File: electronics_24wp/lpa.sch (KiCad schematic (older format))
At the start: 26 parts, among them IC1 ATMEGA328-A, P1 CONN_2, P2 CONN_3X2, U1 SD_CARD, U2 LD1117S33, Y1 RESONATEUR

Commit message: Changed names of kicad files.
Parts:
- C1, C2, C3, C4, C5: symbol C-RESCUE-tca -> C-RESCUE-lpa
- ERR1, FIN1, ON1: symbol LED-RESCUE-tca -> LED-RESCUE-lpa
- IC1: symbol ATMEGA328-A-RESCUE-tca -> ATMEGA328-A-RESCUE-lpa
- R1, R15, R16, R17, R18, R19, R2, R_ERR1, R_FIN1, R_ON1: symbol R-RESCUE-tca -> R-RESCUE-lpa
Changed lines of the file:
@@
 EESchema Schematic File Version 2
-LIBS:tca-rescue
+LIBS:lpa-rescue
 LIBS:power
 LIBS:device
@@
 LIBS:valves
 LIBS:myParts
-LIBS:tca-cache
+LIBS:lpa-cache
 EELAYER 25 0
 EELAYER END
@@
 SS
 $Comp
-L GND-RESCUE-tca #PWR01
+L GND-RESCUE-lpa #PWR01
 U 1 1 5358B074
 P 2450 2800
@@
 $EndComp
 $Comp
-L C-RESCUE-tca C5
+L C-RESCUE-lpa C5
 U 1 1 535704C8
 P 3300 6600
@@
 $EndComp
 $Comp
-L C-RESCUE-tca C3
+L C-RESCUE-lpa C3
 U 1 1 535704B9
 P 1550 6600
@@
 ERR
 $Comp
-L R-RESCUE-tca R_FIN1
+L R-RESCUE-lpa R_FIN1
 U 1 1 5356ED9C
 P 4150 6850
@@
 $EndComp
 $Comp
-L R-RESCUE-tca R_ERR1
+L R-RESCUE-lpa R_ERR1
 U 1 1 5356ED8D
 P 4150 6550
@@
 $EndComp
 $Comp
-L R-RESCUE-tca R_ON1
+L R-RESCUE-lpa R_ON1
 U 1 1 5356ED7E
 P 4150 6250
@@
 ERR
 $Comp
-L LED-RESCUE-tca FIN1
+L LED-RESCUE-lpa FIN1
 U 1 1 5356E78D
 P 4750 6850
@@
 $EndComp
 $Comp
-L LED-RESCUE-tca ERR1
+L LED-RESCUE-lpa ERR1
 U 1 1 5356E77E
 P 4750 6550
@@
 $EndComp
 $Comp
-L LED-RESCUE-tca ON1
+L LED-RESCUE-lpa ON1
 U 1 1 5356E76F
 P 4750 6250
@@
 $EndComp
 $Comp
-L GND-RESCUE-tca #PWR02
+L GND-RESCUE-lpa #PWR02
 U 1 1 5356E577
 P 5100 7300
@@
 VCC
 $Comp
-L GND-RESCUE-tca #PWR03
+L GND-RESCUE-lpa #PWR03
 U 1 1 52166F83
 P 4300 4400
@@
 NoConn ~ 1350 4000
 $Comp
-L C-RESCUE-tca C2
+L C-RESCUE-lpa C2
 U 1 1 52150FEA
 P 1050 3700
@@
 $EndComp
 $Comp
-L C-RESCUE-tca C1
+L C-RESCUE-lpa C1
 U 1 1 52150FDD
 P 1050 3500
@@
 $EndComp
 $Comp
-L GND-RESCUE-tca #PWR04
+L GND-RESCUE-lpa #PWR04
 U 1 1 52150FBD
 P 800 5850
@@
 $EndComp
 $Comp
-L ATMEGA328-A-RESCUE-tca IC1
+L ATMEGA328-A-RESCUE-lpa IC1
 U 1 1 52150E25
 P 2250 4500
@@
 MOSI
 $Comp
-L R-RESCUE-tca R1
+L R-RESCUE-lpa R1
 U 1 1 5214E00C
 P 4500 7600
@@
 VCC
 $Comp
-L GND-RESCUE-tca #PWR05
+L GND-RESCUE-lpa #PWR05
 U 1 1 5214D884
 P 5050 5650
@@
 MISO
 $Comp
-L GND-RESCUE-tca #PWR06
+L GND-RESCUE-lpa #PWR06
 U 1 1 5214D369
 P 1250 6850
@@
 $EndSheet
 $Comp
-L R-RESCUE-tca R2
+L R-RESCUE-lpa R2
 U 1 1 5363149A
 P 6150 2900
@@
 $EndComp
 $Comp
-L C-RESCUE-tca C4
+L C-RESCUE-lpa C4
 U 1 1 53AA0322
 P 2250 6600
@@
 	2450 2150 2350 2150
 $Comp
-L R-RESCUE-tca R15
+L R-RESCUE-lpa R15
 U 1 1 53AA1B37
 P 2750 1400
@@
 $EndComp
 $Comp
-L R-RESCUE-tca R16
+L R-RESCUE-lpa R16
 U 1 1 53AA1B5A
 P 2950 1400
@@
 $EndComp
 $Comp
-L R-RESCUE-tca R17
+L R-RESCUE-lpa R17
 U 1 1 53AA1B60
 P 3150 1400
@@
 $EndComp
 $Comp
-L R-RESCUE-tca R18
+L R-RESCUE-lpa R18
 U 1 1 53AA1B66
 P 3350 1400
@@
 $EndComp
 $Comp
-L R-RESCUE-tca R19
+L R-RESCUE-lpa R19
 U 1 1 53AA1B6C
 P 3550 1400

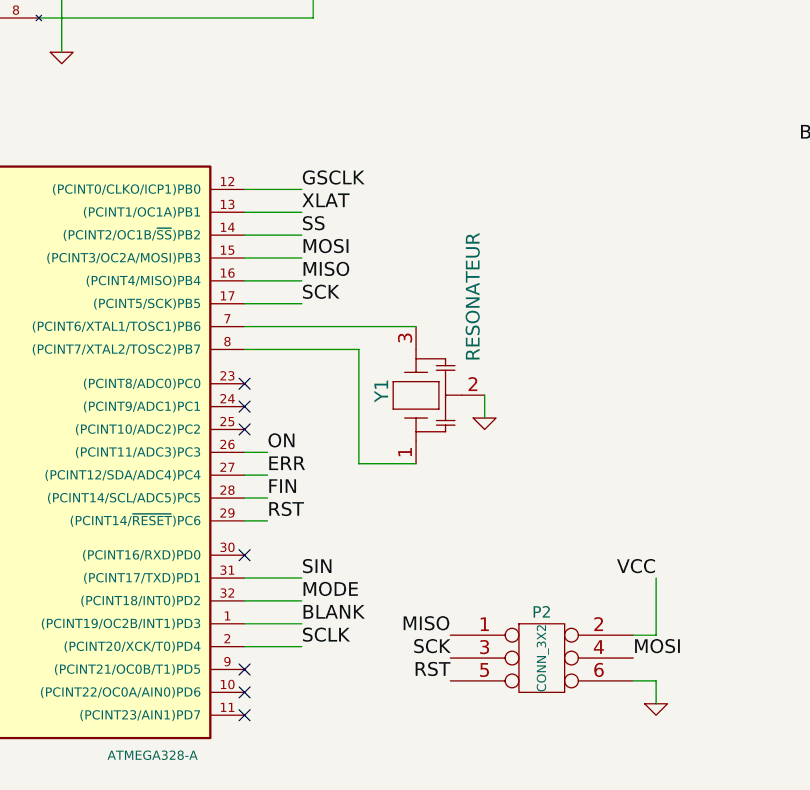
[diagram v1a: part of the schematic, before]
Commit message: Changed board to use quartz oscillator.
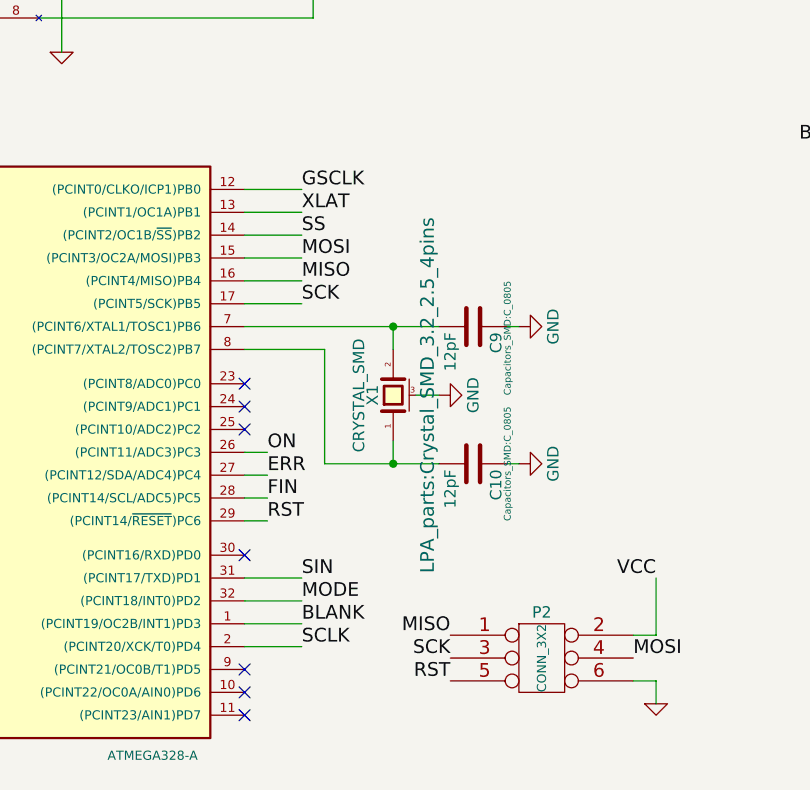
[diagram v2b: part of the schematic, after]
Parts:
- removed Y1: RESONATEUR, crystal_smd, symbol RESONATEUR
- added C10, C9: 12pF, Capacitors_SMD:C_0805, symbol C
- added X1: CRYSTAL_SMD, LPA_parts:Crystal_SMD_3.2_2.5_4pins, symbol CRYSTAL_SMD
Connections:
- net GND: now also C10.1, C9.1, X1.3 (case)
- net at IC1.7 ((PCINT6/XTAL1/TOSC1)PB6): now also C9.2, X1.2
- net at IC1.8 ((PCINT7/XTAL2/TOSC2)PB7): now also C10.2, X1.1
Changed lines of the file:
@@
 Text Label 4850 7600 0    60   ~ 0
 VCC
-$Comp
-L GND-RESCUE-lpa #PWR03
-U 1 1 52166F83
-P 4300 4400
-F 0 "#PWR03" H 4300 4400 30  0001 C CNN
-F 1 "GND" H 4300 4330 30  0001 C CNN
-F 2 "" H 4300 4400 60  0000 C CNN
-F 3 "" H 4300 4400 60  0000 C CNN
-	1    4300 4400
-	1    0    0    -1
-$EndComp
-$Comp
-L RESONATEUR Y1
-U 1 1 52166DFA
-P 4050 4300
-F 0 "Y1" H 4070 4500 60  0000 C CNN
-F 1 "RESONATEUR" H 4480 4100 60  0000 C CNN
-F 2 "crystal_smd" H 4050 4300 60  0001 C CNN
-F 3 "" H 4050 4300 60  0000 C CNN
-	1    4050 4300
-	0    -1   -1   0
-$EndComp
 NoConn ~ 3250 4250
 NoConn ~ 3250 4350
@@
 $EndComp
 $Comp
-L GND-RESCUE-lpa #PWR04
+L GND-RESCUE-lpa #PWR03
 U 1 1 52150FBD
 P 800 5850
-F 0 "#PWR04" H 800 5850 30  0001 C CNN
+F 0 "#PWR03" H 800 5850 30  0001 C CNN
 F 1 "GND" H 800 5780 30  0001 C CNN
 F 2 "" H 800 5850 60  0000 C CNN
@@
 VCC
 $Comp
-L GND-RESCUE-lpa #PWR05
+L GND-RESCUE-lpa #PWR04
 U 1 1 5214D884
 P 5050 5650
-F 0 "#PWR05" H 5050 5650 30  0001 C CNN
+F 0 "#PWR04" H 5050 5650 30  0001 C CNN
 F 1 "GND" H 5050 5580 30  0001 C CNN
 F 2 "" H 5050 5650 60  0000 C CNN
@@
 MISO
 $Comp
-L GND-RESCUE-lpa #PWR06
+L GND-RESCUE-lpa #PWR05
 U 1 1 5214D369
 P 1250 6850
-F 0 "#PWR06" H 1250 6850 30  0001 C CNN
+F 0 "#PWR05" H 1250 6850 30  0001 C CNN
 F 1 "GND" H 1250 6780 30  0001 C CNN
 F 2 "" H 1250 6850 60  0000 C CNN
@@
 	850  3700 800  3700
 Wire Wire Line
-	4300 4300 4300 4400
-Wire Wire Line
-	3750 4600 4000 4600
-Wire Wire Line
-	3750 4100 3750 4600
-Wire Wire Line
-	3250 4100 3750 4100
-Wire Wire Line
-	3250 4000 4000 4000
+	3600 4600 4100 4600
+Wire Wire Line
+	3600 4100 3600 4600
+Wire Wire Line
+	3250 4100 3600 4100
+Wire Wire Line
+	3250 4000 4100 4000
 Connection ~ 800  5500
 Connection ~ 1300 3400
@@
 Wire Wire Line
 	3550 2650 3550 1650
+$Comp
+L C C9
+U 1 1 569716A8
+P 4250 4000
+F 0 "C9" H 4275 4100 50  0000 L CNN
+F 1 "12pF" H 4275 3900 50  0000 L CNN
+F 2 "Capacitors_SMD:C_0805" H 4300 4150 30  0000 C CNN
+F 3 "" H 4250 4000 60  0000 C CNN
+	1    4250 4000
+	0    1    1    0
+$EndComp
+$Comp
+L C C10
+U 1 1 56971787
+P 4250 4600
+F 0 "C10" H 4275 4700 50  0000 L CNN
+F 1 "12pF" H 4275 4500 50  0000 L CNN
+F 2 "Capacitors_SMD:C_0805" H 4250 4750 30  0000 C CNN
+F 3 "" H 4250 4600 60  0000 C CNN
+	1    4250 4600
+	0    1    1    0
+$EndComp
+$Comp
+L GND #PWR06
+U 1 1 569719B9
+P 4450 4000
+F 0 "#PWR06" H 4450 3750 50  0001 C CNN
+F 1 "GND" H 4450 3850 50  0000 C CNN
+F 2 "" H 4450 4000 60  0000 C CNN
+F 3 "" H 4450 4000 60  0000 C CNN
+	1    4450 4000
+	0    -1   -1   0
+$EndComp
+$Comp
+L GND #PWR07
+U 1 1 56971A39
+P 4450 4600
+F 0 "#PWR07" H 4450 4350 50  0001 C CNN
+F 1 "GND" H 4450 4450 50  0000 C CNN
+F 2 "" H 4450 4600 60  0000 C CNN
+F 3 "" H 4450 4600 60  0000 C CNN
+	1    4450 4600
+	0    -1   -1   0
+$EndComp
+Wire Wire Line
+	4400 4000 4450 4000
+Wire Wire Line
+	4400 4600 4450 4600
+$Comp
+L CRYSTAL_SMD X1
+U 1 1 569760FF
+P 3900 4300
+F 0 "X1" H 3900 4390 50  0000 C CNN
+F 1 "CRYSTAL_SMD" H 3650 4450 50  0000 L CNN
+F 2 "LPA_parts:Crystal_SMD_3.2_2.5_4pins" H 3900 4150 60  0000 C CNN
+F 3 "" H 3900 4300 60  0000 C CNN
+	1    3900 4300
+	0    -1   -1   0
+$EndComp
+Wire Wire Line
+	3900 4100 3900 4000
+Connection ~ 3900 4000
+Wire Wire Line
+	3900 4500 3900 4600
+Connection ~ 3900 4600
+$Comp
+L GND #PWR08
+U 1 1 56976406
+P 4100 4300
+F 0 "#PWR08" H 4100 4050 50  0001 C CNN
+F 1 "GND" H 4100 4150 50  0000 C CNN
+F 2 "" H 4100 4300 60  0000 C CNN
+F 3 "" H 4100 4300 60  0000 C CNN
+	1    4100 4300
+	0    -1   -1   0
+$EndComp
+Wire Wire Line
+	4000 4300 4100 4300
 $EndSCHEMATC

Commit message: Streamlined library files for the electronic schematic.
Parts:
- C1, C2, C3, C4, C5: symbol C-RESCUE-lpa -> C
- ERR1, FIN1, ON1: symbol LED-RESCUE-lpa -> LED
- IC1: symbol ATMEGA328-A-RESCUE-lpa -> ATMEGA328-A
- R1, R15, R16, R17, R18, R19, R2, R_ERR1, R_FIN1, R_ON1: symbol R-RESCUE-lpa -> R
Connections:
- net GND: now also ERR1.1 (K), FIN1.1 (K), ON1.1 (K); no longer ERR1.2 (K), FIN1.2 (K), ON1.2 (K)
- net at R_ON1.2: now also ON1.2 (A); no longer ON1.1 (A)
- net at R_ERR1.2: now also ERR1.2 (A); no longer ERR1.1 (A)
- net at R_FIN1.2: now also FIN1.2 (A); no longer FIN1.1 (A)
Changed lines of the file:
@@
 EESchema Schematic File Version 2
-LIBS:lpa-rescue
 LIBS:power
 LIBS:device
@@
 SS
 $Comp
-L GND-RESCUE-lpa #PWR01
+L GND #PWR01
 U 1 1 5358B074
 P 2450 2800
@@
 $EndComp
 $Comp
-L C-RESCUE-lpa C5
+L C C5
 U 1 1 535704C8
 P 3300 6600
@@
 $EndComp
 $Comp
-L C-RESCUE-lpa C3
+L C C3
 U 1 1 535704B9
 P 1550 6600
@@
 ERR
 $Comp
-L R-RESCUE-lpa R_FIN1
+L R R_FIN1
 U 1 1 5356ED9C
 P 4150 6850
@@
 $EndComp
 $Comp
-L R-RESCUE-lpa R_ERR1
+L R R_ERR1
 U 1 1 5356ED8D
 P 4150 6550
@@
 $EndComp
 $Comp
-L R-RESCUE-lpa R_ON1
+L R R_ON1
 U 1 1 5356ED7E
 P 4150 6250
@@
 ERR
 $Comp
-L LED-RESCUE-lpa FIN1
+L LED FIN1
 U 1 1 5356E78D
 P 4750 6850
@@
 F 3 "~" H 4750 6850 60  0000 C CNN
 	1    4750 6850
-	1    0    0    -1
-$EndComp
-$Comp
-L LED-RESCUE-lpa ERR1
+	-1   0    0    -1
+$EndComp
+$Comp
+L LED ERR1
 U 1 1 5356E77E
 P 4750 6550
@@
 F 3 "~" H 4750 6550 60  0000 C CNN
 	1    4750 6550
-	1    0    0    -1
-$EndComp
-$Comp
-L LED-RESCUE-lpa ON1
+	-1   0    0    -1
+$EndComp
+$Comp
+L LED ON1
 U 1 1 5356E76F
 P 4750 6250
@@
 F 3 "~" H 4750 6250 60  0000 C CNN
 	1    4750 6250
-	1    0    0    -1
-$EndComp
-$Comp
-L GND-RESCUE-lpa #PWR02
+	-1   0    0    -1
+$EndComp
+$Comp
+L GND #PWR02
 U 1 1 5356E577
 P 5100 7300
@@
 NoConn ~ 1350 4000
 $Comp
-L C-RESCUE-lpa C2
+L C C2
 U 1 1 52150FEA
 P 1050 3700
@@
 $EndComp
 $Comp
-L C-RESCUE-lpa C1
+L C C1
 U 1 1 52150FDD
 P 1050 3500
@@
 $EndComp
 $Comp
-L GND-RESCUE-lpa #PWR03
+L GND #PWR03
 U 1 1 52150FBD
 P 800 5850
@@
 $EndComp
 $Comp
-L ATMEGA328-A-RESCUE-lpa IC1
+L ATMEGA328-A IC1
 U 1 1 52150E25
 P 2250 4500
@@
 MOSI
 $Comp
-L R-RESCUE-lpa R1
+L R R1
 U 1 1 5214E00C
 P 4500 7600
@@
 VCC
 $Comp
-L GND-RESCUE-lpa #PWR04
+L GND #PWR04
 U 1 1 5214D884
 P 5050 5650
@@
 MISO
 $Comp
-L GND-RESCUE-lpa #PWR05
+L GND #PWR05
 U 1 1 5214D369
 P 1250 6850
@@
 $EndSheet
 $Comp
-L R-RESCUE-lpa R2
+L R R2
 U 1 1 5363149A
 P 6150 2900
@@
 $EndComp
 $Comp
-L C-RESCUE-lpa C4
+L C C4
 U 1 1 53AA0322
 P 2250 6600
@@
 	2350 1950 4000 1950
 Wire Wire Line
-	3300 6400 3300 6350
+	3300 6350 3300 6450
 Connection ~ 3300 6350
 Wire Wire Line
@@
 Connection ~ 1550 6350
 Wire Wire Line
-	1550 6400 1550 6350
+	1550 6350 1550 6450
 Connection ~ 1250 6500
 Wire Wire Line
@@
 	1150 6500 1450 6500
 Wire Wire Line
-	4750 7600 4850 7600
+	4650 7600 4850 7600
 Connection ~ 4200 7200
 Wire Wire Line
 	4200 7600 4200 7200
 Wire Wire Line
-	4250 7600 4200 7600
-Wire Wire Line
-	3700 6850 3900 6850
-Wire Wire Line
-	3700 6550 3900 6550
-Wire Wire Line
-	3700 6250 3900 6250
+	4200 7600 4350 7600
+Wire Wire Line
+	3700 6850 4000 6850
+Wire Wire Line
+	3700 6550 4000 6550
+Wire Wire Line
+	3700 6250 4000 6250
 Connection ~ 5100 7200
 Wire Wire Line
 	5100 7200 4850 7200
 Connection ~ 5100 6850
-Wire Wire Line
-	5100 6850 4950 6850
 Connection ~ 5100 6550
 Wire Wire Line
-	4950 6550 5100 6550
-Wire Wire Line
 	5100 6250 5100 7300
 Wire Wire Line
-	4950 6250 5100 6250
-Wire Wire Line
-	4400 6850 4550 6850
-Wire Wire Line
-	4400 6550 4550 6550
-Wire Wire Line
-	4400 6250 4550 6250
-Wire Wire Line
 	3350 4850 3250 4850
 Wire Wire Line
@@
 	3250 5100 3500 5100
 Wire Wire Line
-	800  3500 850  3500
+	800  3500 900  3500
 Connection ~ 800  3700
 Wire Wire Line
-	850  3700 800  3700
+	800  3700 900  3700
 Wire Wire Line
 	3600 4600 4100 4600
@@
 Connection ~ 1300 3500
 Wire Wire Line
-	1250 3700 1350 3700
+	1200 3700 1350 3700
 Wire Wire Line
 	1300 3300 1300 3700
@@
 	1350 3400 1300 3400
 Wire Wire Line
-	1250 3500 1350 3500
+	1200 3500 1350 3500
 Wire Wire Line
 	800  3500 800  5850
@@
 	4950 5350 5050 5350
 Wire Wire Line
-	6150 2650 6150 2550
+	6150 2550 6150 2750
 Wire Wire Line
 	5950 3200 6800 3200
@@
 	9050 3250 9200 3250
 Wire Wire Line
-	6150 3150 6150 3200
+	6150 3050 6150 3200
 Connection ~ 6150 3200
 Wire Wire Line
 	2200 6350 2450 6350
 Wire Wire Line
-	2250 6400 2250 6350
+	2250 6350 2250 6450
 Connection ~ 2250 6350
 Wire Wire Line
@@
 	2450 2150 2350 2150
 $Comp
-L R-RESCUE-lpa R15
+L R R15
 U 1 1 53AA1B37
 P 2750 1400
@@
 $EndComp
 $Comp
-L R-RESCUE-lpa R16
+L R R16
 U 1 1 53AA1B5A
 P 2950 1400
@@
 $EndComp
 $Comp
-L R-RESCUE-lpa R17
+L R R17
 U 1 1 53AA1B60
 P 3150 1400
@@
 $EndComp
 $Comp
-L R-RESCUE-lpa R18
+L R R18
 U 1 1 53AA1B66
 P 3350 1400
@@
 $EndComp
 $Comp
-L R-RESCUE-lpa R19
+L R R19
 U 1 1 53AA1B6C
 P 3550 1400
@@
 Connection ~ 2550 1150
 Wire Wire Line
-	2750 1650 2750 1850
+	2750 1550 2750 1850
 Wire Wire Line
 	2350 2450 2450 2450
@@
 	2550 2250 2350 2250
 Wire Wire Line
-	2950 1650 2950 1950
+	2950 1550 2950 1950
 Connection ~ 2950 1950
 Wire Wire Line
-	3150 1650 3150 2050
+	3150 1550 3150 2050
 Connection ~ 3150 2050
 Wire Wire Line
-	3350 1650 3350 2550
+	3350 1550 3350 2550
 Connection ~ 3350 2550
 Wire Wire Line
-	2350 2650 3550 2650
-Wire Wire Line
-	3550 2650 3550 1650
+	3550 1550 3550 2650
 $Comp
 L C C9
@@
 F 0 "C9" H 4275 4100 50  0000 L CNN
 F 1 "12pF" H 4275 3900 50  0000 L CNN
-F 2 "Capacitors_SMD:C_0805" H 4300 4150 30  0000 C CNN
+F 2 "Capacitors_SMD:C_0805" H 4300 4150 30  0001 C CNN
 F 3 "" H 4250 4000 60  0000 C CNN
 	1    4250 4000
@@
 F 0 "C10" H 4275 4700 50  0000 L CNN
 F 1 "12pF" H 4275 4500 50  0000 L CNN
-F 2 "Capacitors_SMD:C_0805" H 4250 4750 30  0000 C CNN
+F 2 "Capacitors_SMD:C_0805" H 4250 4750 30  0001 C CNN
 F 3 "" H 4250 4600 60  0000 C CNN
 	1    4250 4600
@@
 F 0 "X1" H 3900 4390 50  0000 C CNN
 F 1 "CRYSTAL_SMD" H 3650 4450 50  0000 L CNN
-F 2 "LPA_parts:Crystal_SMD_3.2_2.5_4pins" H 3900 4150 60  0000 C CNN
+F 2 "LPA_parts:Crystal_SMD_3.2_2.5_4pins" H 3900 4150 60  0001 C CNN
 F 3 "" H 3900 4300 60  0000 C CNN
 	1    3900 4300
@@
 Wire Wire Line
 	4000 4300 4100 4300
+Wire Wire Line
+	3550 1150 3550 1250
+Wire Wire Line
+	3350 1250 3350 1150
+Wire Wire Line
+	3150 1150 3150 1250
+Wire Wire Line
+	2950 1250 2950 1150
+Wire Wire Line
+	2750 1150 2750 1250
+Wire Wire Line
+	1550 6750 1550 6800
+Wire Wire Line
+	2250 6750 2250 6800
+Wire Wire Line
+	3300 6800 3300 6750
+Wire Wire Line
+	4950 6250 5100 6250
+Wire Wire Line
+	4950 6550 5100 6550
+Wire Wire Line
+	5100 6850 4950 6850
+Wire Wire Line
+	4300 6850 4550 6850
+Wire Wire Line
+	4300 6550 4550 6550
+Wire Wire Line
+	4300 6250 4550 6250
+Wire Wire Line
+	3550 2650 2350 2650
 $EndSCHEMATC

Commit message: Streamlined layout libraries.
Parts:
- C1, C2, C5, ERR1, FIN1, ON1, R1, R2, R_ERR1, R_FIN1, R_ON1: footprint SM0805 -> LPA_parts:SM0805
- C10, C9: footprint Capacitors_SMD:C_0805 -> LPA_parts:SM0805
- IC1: footprint TQFP32_FIXED -> LPA_parts:ATMEGA328
- P1: footprint PIN_ARRAY_2X1_3960um -> LPA_parts:CONNECTOR_2X1_3960um
- R15, R16, R17, R18, R19: footprint ~ -> LPA_parts:SM0805
- RESET1: footprint SW_PUSH_SMD -> LPA_parts:SW_PUSH_SMD
- U1: footprint SD_CONN -> LPA_parts:SD_CARD_SOCKET
- X1: footprint LPA_parts:Crystal_SMD_3.2_2.5_4pins -> LPA_parts:CRYSTAL_SMD_3.2_2.5_4pins
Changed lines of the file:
@@
 F 0 "U1" H 1700 1750 60  0000 C CNN
 F 1 "SD_CARD" H 1700 1850 60  0000 C CNN
-F 2 "SD_CONN" H 1950 2050 60  0001 C CNN
+F 2 "LPA_parts:SD_CARD_SOCKET" H 1950 2050 60  0001 C CNN
 F 3 "" H 1950 2050 60  0000 C CNN
 	1    1950 2050
@@
 F 0 "C5" H 3300 6700 40  0000 L CNN
 F 1 "10uF" H 3306 6515 40  0000 L CNN
-F 2 "SM0805" H 3338 6450 30  0001 C CNN
+F 2 "LPA_parts:SM0805" H 3338 6450 30  0001 C CNN
 F 3 "~" H 3300 6600 60  0000 C CNN
 	1    3300 6600
@@
 F 0 "R_FIN1" V 4230 6850 40  0000 C CNN
 F 1 "330" V 4157 6851 40  0000 C CNN
-F 2 "SM0805" V 4080 6850 30  0001 C CNN
+F 2 "LPA_parts:SM0805" V 4080 6850 30  0001 C CNN
 F 3 "~" H 4150 6850 30  0000 C CNN
 	1    4150 6850
@@
 F 0 "R_ERR1" V 4230 6550 40  0000 C CNN
 F 1 "330" V 4157 6551 40  0000 C CNN
-F 2 "SM0805" V 4080 6550 30  0001 C CNN
+F 2 "LPA_parts:SM0805" V 4080 6550 30  0001 C CNN
 F 3 "~" H 4150 6550 30  0000 C CNN
 	1    4150 6550
@@
 F 0 "R_ON1" V 4230 6250 40  0000 C CNN
 F 1 "330" V 4157 6251 40  0000 C CNN
-F 2 "SM0805" V 4080 6250 30  0001 C CNN
+F 2 "LPA_parts:SM0805" V 4080 6250 30  0001 C CNN
 F 3 "~" H 4150 6250 30  0000 C CNN
 	1    4150 6250
@@
 F 0 "FIN1" H 4750 6950 50  0000 C CNN
 F 1 "LED" H 4750 6750 50  0000 C CNN
-F 2 "SM0805" H 4750 6850 60  0001 C CNN
+F 2 "LPA_parts:SM0805" H 4750 6850 60  0001 C CNN
 F 3 "~" H 4750 6850 60  0000 C CNN
 	1    4750 6850
@@
 F 0 "ERR1" H 4750 6650 50  0000 C CNN
 F 1 "LED" H 4750 6450 50  0000 C CNN
-F 2 "SM0805" H 4750 6550 60  0001 C CNN
+F 2 "LPA_parts:SM0805" H 4750 6550 60  0001 C CNN
 F 3 "~" H 4750 6550 60  0000 C CNN
 	1    4750 6550
@@
 F 0 "ON1" H 4750 6350 50  0000 C CNN
 F 1 "LED" H 4750 6150 50  0000 C CNN
-F 2 "SM0805" H 4750 6250 60  0001 C CNN
+F 2 "LPA_parts:SM0805" H 4750 6250 60  0001 C CNN
 F 3 "~" H 4750 6250 60  0000 C CNN
 	1    4750 6250
@@
 F 0 "RESET1" H 4700 7310 50  0000 C CNN
 F 1 "SW_PUSH" H 4550 7120 50  0000 C CNN
-F 2 "SW_PUSH_SMD" H 4550 7200 60  0001 C CNN
+F 2 "LPA_parts:SW_PUSH_SMD" H 4550 7200 60  0001 C CNN
 F 3 "~" H 4550 7200 60  0000 C CNN
 	1    4550 7200
@@
 F 0 "C2" H 1050 3800 40  0000 L CNN
 F 1 "0.1 uF" H 1056 3615 40  0000 L CNN
-F 2 "SM0805" H 1088 3550 30  0001 C CNN
+F 2 "LPA_parts:SM0805" H 1088 3550 30  0001 C CNN
 F 3 "~" H 1050 3700 60  0000 C CNN
 	1    1050 3700
@@
 F 0 "C1" H 1050 3600 40  0000 L CNN
 F 1 "0.1 uF" H 1056 3415 40  0000 L CNN
-F 2 "SM0805" H 1088 3350 30  0001 C CNN
+F 2 "LPA_parts:SM0805" H 1088 3350 30  0001 C CNN
 F 3 "~" H 1050 3500 60  0000 C CNN
 	1    1050 3500
@@
 F 0 "IC1" H 1500 5750 40  0000 L BNN
 F 1 "ATMEGA328-A" H 2650 3100 40  0000 L BNN
-F 2 "TQFP32_FIXED" H 2250 4500 30  0001 C CIN
+F 2 "LPA_parts:ATMEGA328" H 2250 4500 30  0001 C CIN
 F 3 "" H 2250 4500 60  0000 C CNN
 	1    2250 4500
@@
 F 0 "R1" V 4580 7600 40  0000 C CNN
 F 1 "10K" V 4507 7601 40  0000 C CNN
-F 2 "SM0805" V 4430 7600 30  0001 C CNN
+F 2 "LPA_parts:SM0805" V 4430 7600 30  0001 C CNN
 F 3 "~" H 4500 7600 30  0000 C CNN
 	1    4500 7600
@@
 F 0 "P1" V 750 6600 40  0000 C CNN
 F 1 "CONN_2" V 850 6600 40  0000 C CNN
-F 2 "PIN_ARRAY_2X1_3960um" H 800 6600 60  0001 C CNN
+F 2 "LPA_parts:CONNECTOR_2X1_3960um" H 800 6600 60  0001 C CNN
 F 3 "" H 800 6600 60  0000 C CNN
 	1    800  6600
@@
 F 0 "R2" V 6230 2900 40  0000 C CNN
 F 1 "10K" V 6157 2901 40  0000 C CNN
-F 2 "SM0805" V 6080 2900 30  0001 C CNN
+F 2 "LPA_parts:SM0805" V 6080 2900 30  0001 C CNN
 F 3 "~" H 6150 2900 30  0000 C CNN
 	1    6150 2900
@@
 F 0 "R15" V 2830 1400 40  0000 C CNN
 F 1 "50k" V 2757 1401 40  0000 C CNN
-F 2 "~" V 2680 1400 30  0000 C CNN
+F 2 "LPA_parts:SM0805" V 2680 1400 30  0001 C CNN
 F 3 "~" H 2750 1400 30  0000 C CNN
 	1    2750 1400
@@
 F 0 "R16" V 3030 1400 40  0000 C CNN
 F 1 "50k" V 2957 1401 40  0000 C CNN
-F 2 "~" V 2880 1400 30  0000 C CNN
+F 2 "LPA_parts:SM0805" V 2880 1400 30  0001 C CNN
 F 3 "~" H 2950 1400 30  0000 C CNN
 	1    2950 1400
@@
 F 0 "R17" V 3230 1400 40  0000 C CNN
 F 1 "50k" V 3157 1401 40  0000 C CNN
-F 2 "~" V 3080 1400 30  0000 C CNN
+F 2 "LPA_parts:SM0805" V 3080 1400 30  0001 C CNN
 F 3 "~" H 3150 1400 30  0000 C CNN
 	1    3150 1400
@@
 F 0 "R18" V 3430 1400 40  0000 C CNN
 F 1 "50k" V 3357 1401 40  0000 C CNN
-F 2 "~" V 3280 1400 30  0000 C CNN
+F 2 "LPA_parts:SM0805" V 3280 1400 30  0001 C CNN
 F 3 "~" H 3350 1400 30  0000 C CNN
 	1    3350 1400
@@
 F 0 "R19" V 3630 1400 40  0000 C CNN
 F 1 "50k" V 3557 1401 40  0000 C CNN
-F 2 "~" V 3480 1400 30  0000 C CNN
+F 2 "LPA_parts:SM0805" V 3480 1400 30  0001 C CNN
 F 3 "~" H 3550 1400 30  0000 C CNN
 	1    3550 1400
@@
 F 0 "C9" H 4275 4100 50  0000 L CNN
 F 1 "12pF" H 4275 3900 50  0000 L CNN
-F 2 "Capacitors_SMD:C_0805" H 4300 4150 30  0001 C CNN
+F 2 "LPA_parts:SM0805" H 4300 4150 30  0001 C CNN
 F 3 "" H 4250 4000 60  0000 C CNN
 	1    4250 4000
@@
 F 0 "C10" H 4275 4700 50  0000 L CNN
 F 1 "12pF" H 4275 4500 50  0000 L CNN
-F 2 "Capacitors_SMD:C_0805" H 4250 4750 30  0001 C CNN
+F 2 "LPA_parts:SM0805" H 4250 4750 30  0001 C CNN
 F 3 "" H 4250 4600 60  0000 C CNN
 	1    4250 4600
@@
 F 0 "X1" H 3900 4390 50  0000 C CNN
 F 1 "CRYSTAL_SMD" H 3650 4450 50  0000 L CNN
-F 2 "LPA_parts:Crystal_SMD_3.2_2.5_4pins" H 3900 4150 60  0001 C CNN
+F 2 "LPA_parts:CRYSTAL_SMD_3.2_2.5_4pins" H 3900 4150 60  0001 C CNN
 F 3 "" H 3900 4300 60  0000 C CNN
 	1    3900 4300

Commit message: Changed reset button layout for standard library item.
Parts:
- RESET1: footprint LPA_parts:SW_PUSH_SMD -> Buttons_Switches_SMD:SW_SPST_PTS645
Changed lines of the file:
@@
 F 0 "RESET1" H 4700 7310 50  0000 C CNN
 F 1 "SW_PUSH" H 4550 7120 50  0000 C CNN
-F 2 "LPA_parts:SW_PUSH_SMD" H 4550 7200 60  0001 C CNN
+F 2 "Buttons_Switches_SMD:SW_SPST_PTS645" H 4550 7200 60  0001 C CNN
 F 3 "~" H 4550 7200 60  0000 C CNN
 	1    4550 7200
